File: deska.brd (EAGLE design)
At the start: 100 x 80 mm, 17 parts, among them Q1 BC547, Q2 BC547

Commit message: +
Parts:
- UART: device con-wago-508:W237-132 -> con-wago-508:W237-3E
- moved RELAY 5.08 mm to (5.08, 14.0)
- moved UART 2.54 mm to (5.08, 26.7)
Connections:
- removed net +3V3: BUZZER.2, I2C.2, R1.2, R2.2, R3.2, RELAY.2, TIN.1, TOUT.1, TUT.1, U$1.RAW
- removed net N$8: TIN.2, TOUT.3, TUT.3
- new net +5V: I2C.2, LED.2, R1.2, R2.2, R3.2, RELAY.2, TIN.1, TOUT.1, TUT.1, U$1.RAW
- net GND: now also BUZZER.2, TIN.2, TOUT.3, TUT.3, UART.1; no longer LED.2
- net N$10: now also UART.3; no longer UART.2
- net N$9: now also UART.2; no longer UART.1
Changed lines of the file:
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@@
 <element name="R2" library="rcl" package="0207/7" value="4k7" x="11.43" y="60.96" rot="R90"/>
 <element name="R3" library="rcl" package="0207/7" value="4k7" x="11.43" y="45.72" rot="R90"/>
-<element name="RELAY" library="con-wago-508" package="W237-132" value="" x="5.08" y="19.05" rot="R270">
-<attribute name="OC_NEWARK" value="unknown" x="5.08" y="19.05" size="1.778" layer="27" rot="R270" display="off"/>
-<attribute name="MPN" value="" x="5.08" y="19.05" size="1.778" layer="27" rot="R270" display="off"/>
-<attribute name="MF" value="" x="5.08" y="19.05" size="1.778" layer="27" rot="R270" display="off"/>
-<attribute name="OC_FARNELL" value="unknown" x="5.08" y="19.05" size="1.778" layer="27" rot="R270" display="off"/>
+<element name="RELAY" library="con-wago-508" package="W237-132" value="" x="5.08" y="13.97" rot="R270">
+<attribute name="OC_NEWARK" value="unknown" x="5.08" y="13.97" size="1.778" layer="27" rot="R270" display="off"/>
+<attribute name="MPN" value="" x="5.08" y="13.97" size="1.778" layer="27" rot="R270" display="off"/>
+<attribute name="MF" value="" x="5.08" y="13.97" size="1.778" layer="27" rot="R270" display="off"/>
+<attribute name="OC_FARNELL" value="unknown" x="5.08" y="13.97" size="1.778" layer="27" rot="R270" display="off"/>
 </element>
 <element name="LED" library="con-wago-508" package="W237-132" value="" x="45.72" y="22.86" rot="R270">
@@
 <attribute name="OC_FARNELL" value="unknown" x="5.08" y="41.91" size="1.778" layer="27" rot="R270" display="off"/>
 </element>
-<element name="UART" library="con-wago-508" package="W237-132" value="" x="5.08" y="29.21" rot="R270">
-<attribute name="OC_NEWARK" value="unknown" x="5.08" y="29.21" size="1.778" layer="27" rot="R270" display="off"/>
-<attribute name="MPN" value="" x="5.08" y="29.21" size="1.778" layer="27" rot="R270" display="off"/>
-<attribute name="MF" value="" x="5.08" y="29.21" size="1.778" layer="27" rot="R270" display="off"/>
-<attribute name="OC_FARNELL" value="unknown" x="5.08" y="29.21" size="1.778" layer="27" rot="R270" display="off"/>
-</element>
 <element name="Q1" library="transistor-npn" package="TO92" value="BC547" x="31.75" y="11.43"/>
 <element name="Q2" library="transistor-npn" package="TO92" value="BC547" x="22.86" y="11.43"/>
@@
 <attribute name="OC_FARNELL" value="unknown" x="45.72" y="50.8" size="1.778" layer="27" rot="R90" display="off"/>
 </element>
+<element name="UART" library="con-wago-508" package="W237-3E" value="" x="5.08" y="26.67" rot="R270">
+<attribute name="OC_NEWARK" value="unknown" x="5.08" y="26.67" size="1.778" layer="27" rot="R270" display="off"/>
+<attribute name="MPN" value="" x="5.08" y="26.67" size="1.778" layer="27" rot="R270" display="off"/>
+<attribute name="MF" value="" x="5.08" y="26.67" size="1.778" layer="27" rot="R270" display="off"/>
+<attribute name="OC_FARNELL" value="unknown" x="5.08" y="26.67" size="1.778" layer="27" rot="R270" display="off"/>
+</element>
 </elements>
 <signals>
 <signal name="N$1">
 <contactref element="U$1" pad="D2"/>
+<contactref element="TIN" pad="3"/>
 <contactref element="R1" pad="1"/>
-<contactref element="TIN" pad="3"/>
-<wire x1="11.43" y1="74.93" x2="4.445" y2="67.31" width="0" layer="19" extent="1-1"/>
-<wire x1="19.05" y1="39.37" x2="11.43" y2="74.93" width="0" layer="19" extent="1-1"/>
+<wire x1="4.445" y1="67.31" x2="11.43" y2="74.93" width="0" layer="19" extent="1-1"/>
+<wire x1="19.05" y1="39.37" x2="4.445" y2="67.31" width="0" layer="19" extent="1-1"/>
 </signal>
 <signal name="N$2">
 <contactref element="U$1" pad="D4"/>
+<contactref element="TOUT" pad="2"/>
 <contactref element="R2" pad="1"/>
-<contactref element="TOUT" pad="2"/>
-<wire x1="11.43" y1="57.15" x2="4.445" y2="57.15" width="0" layer="19" extent="1-1"/>
+<wire x1="4.445" y1="57.15" x2="11.43" y2="57.15" width="0" layer="19" extent="1-1"/>
 <wire x1="19.05" y1="34.29" x2="11.43" y2="57.15" width="0" layer="19" extent="1-1"/>
 </signal>
 <signal name="N$3">
 <contactref element="U$1" pad="D5"/>
+<contactref element="TUT" pad="2"/>
 <contactref element="R3" pad="1"/>
-<contactref element="TUT" pad="2"/>
-<wire x1="11.43" y1="41.91" x2="4.445" y2="41.91" width="0" layer="19" extent="1-1"/>
+<wire x1="4.445" y1="41.91" x2="11.43" y2="41.91" width="0" layer="19" extent="1-1"/>
 <wire x1="19.05" y1="31.75" x2="11.43" y2="41.91" width="0" layer="19" extent="1-1"/>
-</signal>
-<signal name="+3V3">
-<contactref element="R3" pad="2"/>
-<contactref element="R2" pad="2"/>
-<contactref element="R1" pad="2"/>
-<contactref element="U$1" pad="RAW"/>
-<contactref element="TIN" pad="1"/>
-<contactref element="TOUT" pad="1"/>
-<contactref element="TUT" pad="1"/>
-<contactref element="RELAY" pad="2"/>
-<contactref element="BUZZER" pad="2"/>
-<contactref element="I2C" pad="2"/>
-<wire x1="45.085" y1="30.48" x2="34.29" y2="49.53" width="0" layer="19" extent="1-1"/>
-<wire x1="11.43" y1="49.53" x2="34.29" y2="49.53" width="0" layer="19" extent="1-1"/>
-<wire x1="4.445" y1="46.99" x2="11.43" y2="49.53" width="0" layer="19" extent="1-1"/>
-<wire x1="4.445" y1="62.23" x2="11.43" y2="49.53" width="0" layer="19" extent="1-1"/>
-<wire x1="11.43" y1="64.77" x2="4.445" y2="62.23" width="0" layer="19" extent="1-1"/>
-<wire x1="11.43" y1="67.31" x2="11.43" y2="64.77" width="0" layer="19" extent="1-1"/>
-<wire x1="4.445" y1="77.47" x2="11.43" y2="67.31" width="0" layer="19" extent="1-1"/>
-<wire x1="4.445" y1="16.51" x2="4.445" y2="46.99" width="0" layer="19" extent="1-1"/>
-<wire x1="46.355" y1="48.26" x2="4.445" y2="16.51" width="0" layer="19" extent="1-1"/>
 </signal>
 <signal name="GND">
 <contactref element="U$1" pad="GND"/>
-<contactref element="LED" pad="2"/>
+<contactref element="UART" pad="1"/>
+<contactref element="BUZZER" pad="2"/>
+<contactref element="I2C" pad="1"/>
 <contactref element="Q2" pad="1"/>
 <contactref element="Q1" pad="1"/>
-<contactref element="I2C" pad="1"/>
-<wire x1="45.085" y1="20.32" x2="34.29" y2="46.99" width="0" layer="19" extent="1-1"/>
-<wire x1="33.02" y1="11.43" x2="45.085" y2="20.32" width="0" layer="19" extent="1-1"/>
+<contactref element="TIN" pad="2"/>
+<contactref element="TOUT" pad="3"/>
+<contactref element="TUT" pad="3"/>
+<wire x1="34.29" y1="46.99" x2="46.355" y2="43.18" width="0" layer="19" extent="1-1"/>
+<wire x1="45.085" y1="30.48" x2="46.355" y2="43.18" width="0" layer="19" extent="1-1"/>
+<wire x1="33.02" y1="11.43" x2="45.085" y2="30.48" width="0" layer="19" extent="1-1"/>
 <wire x1="24.13" y1="11.43" x2="33.02" y2="11.43" width="0" layer="19" extent="1-1"/>
-<wire x1="46.355" y1="43.18" x2="24.13" y2="11.43" width="0" layer="19" extent="1-1"/>
+<wire x1="4.445" y1="31.75" x2="24.13" y2="11.43" width="0" layer="19" extent="1-1"/>
+<wire x1="4.445" y1="36.83" x2="4.445" y2="31.75" width="0" layer="19" extent="1-1"/>
+<wire x1="4.445" y1="52.07" x2="4.445" y2="36.83" width="0" layer="19" extent="1-1"/>
+<wire x1="4.445" y1="72.39" x2="4.445" y2="52.07" width="0" layer="19" extent="1-1"/>
 </signal>
 <signal name="N$5">
@@
 <wire x1="45.085" y1="25.4" x2="26.67" y2="16.51" width="0" layer="19" extent="1-1"/>
 </signal>
-<signal name="N$8">
-<contactref element="TIN" pad="2"/>
-<contactref element="TOUT" pad="3"/>
-<contactref element="TUT" pad="3"/>
-<wire x1="4.445" y1="52.07" x2="4.445" y2="36.83" width="0" layer="19" extent="1-1"/>
-<wire x1="4.445" y1="72.39" x2="4.445" y2="52.07" width="0" layer="19" extent="1-1"/>
-</signal>
 <signal name="N$9">
-<contactref element="UART" pad="1"/>
 <contactref element="U$1" pad="TX0"/>
-<wire x1="19.05" y1="49.53" x2="4.445" y2="31.75" width="0" layer="19" extent="1-1"/>
+<contactref element="UART" pad="2"/>
+<wire x1="4.445" y1="26.67" x2="19.05" y2="49.53" width="0" layer="19" extent="1-1"/>
 </signal>
 <signal name="N$10">
-<contactref element="UART" pad="2"/>
 <contactref element="U$1" pad="RX1"/>
-<wire x1="19.05" y1="46.99" x2="4.445" y2="26.67" width="0" layer="19" extent="1-1"/>
+<contactref element="UART" pad="3"/>
+<wire x1="4.445" y1="21.59" x2="19.05" y2="46.99" width="0" layer="19" extent="1-1"/>
 </signal>
 <signal name="N$12">
@@
 <contactref element="RELAY" pad="1"/>
 <contactref element="Q2" pad="3"/>
-<wire x1="21.59" y1="11.43" x2="4.445" y2="21.59" width="0" layer="19" extent="1-1"/>
+<wire x1="21.59" y1="11.43" x2="4.445" y2="16.51" width="0" layer="19" extent="1-1"/>
 </signal>
 <signal name="N$15">
@@
 <wire x1="30.48" y1="24.13" x2="34.29" y2="29.21" width="0" layer="19" extent="1-1"/>
 </signal>
+<signal name="+5V">
+<contactref element="RELAY" pad="2"/>
+<contactref element="LED" pad="2"/>
+<contactref element="R1" pad="2"/>
+<contactref element="R3" pad="2"/>
+<contactref element="R2" pad="2"/>
+<contactref element="TIN" pad="1"/>
+<contactref element="TUT" pad="1"/>
+<contactref element="TOUT" pad="1"/>
+<contactref element="U$1" pad="RAW"/>
+<contactref element="I2C" pad="2"/>
+<wire x1="34.29" y1="49.53" x2="46.355" y2="48.26" width="0" layer="19" extent="1-1"/>
+<wire x1="11.43" y1="49.53" x2="34.29" y2="49.53" width="0" layer="19" extent="1-1"/>
+<wire x1="4.445" y1="46.99" x2="11.43" y2="49.53" width="0" layer="19" extent="1-1"/>
+<wire x1="4.445" y1="62.23" x2="11.43" y2="49.53" width="0" layer="19" extent="1-1"/>
+<wire x1="11.43" y1="64.77" x2="4.445" y2="62.23" width="0" layer="19" extent="1-1"/>
+<wire x1="11.43" y1="67.31" x2="11.43" y2="64.77" width="0" layer="19" extent="1-1"/>
+<wire x1="4.445" y1="77.47" x2="11.43" y2="67.31" width="0" layer="19" extent="1-1"/>
+<wire x1="45.085" y1="20.32" x2="46.355" y2="48.26" width="0" layer="19" extent="1-1"/>
+<wire x1="4.445" y1="11.43" x2="4.445" y2="46.99" width="0" layer="19" extent="1-1"/>
+</signal>
 </signals>

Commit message: zmeny
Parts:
- removed I2C: (no value), con-wago-508:W237-4P
- added COMMUNIT: (no value), con-wago-508:W237-132
- added I2CDISP, I2CHOUR, I2CKEYB, LEDDISP: (no value), con-wago-508:W237-4P
- moved UART 53.8 mm to (22.9, 77.5), turned to 180 degrees
- moved BUZZER 46.5 mm to (7.62, 6.35)
- moved LED 38.6 mm to (7.62, 16.5)
- moved RELAY 13.0 mm to (7.62, 26.7)
- moved R2 10.5 mm to (14.0, 50.8), turned to 270 degrees
- moved R3 10.5 mm to (14.0, 35.6), turned to 270 degrees
- moved R4 10.2 mm to (16.5, 21.6)
- moved R6 10.2 mm to (40.6, 20.3)
- moved R1 6.84 mm to (14.0, 64.8)
- moved R5 5.12 mm to (25.4, 21.0)
- moved TIN 3.59 mm to (7.62, 69.8)
- moved TOUT 3.59 mm to (7.62, 54.6)
- moved TUT 3.59 mm to (7.62, 39.4)
- moved U$1 2.84 mm to (30.5, 38.1)
- moved Q1 2.84 mm to (34.3, 12.7)
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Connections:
- new net N$17: COMMUNIT.2, U$1.A0
- new net N$8: COMMUNIT.1, U$1.A1
- net +5V: now also I2CDISP.2, I2CHOUR.2, I2CKEYB.2, LEDDISP.2; no longer I2C.2
- net GND: now also I2CDISP.1, I2CHOUR.1, I2CKEYB.1, LEDDISP.1, TIN.3; no longer I2C.1, TIN.2
- net N$1: now also TIN.2; no longer TIN.3
- net N$11: now also I2CDISP.4, I2CHOUR.4, I2CKEYB.4, LEDDISP.4; no longer I2C.4
- net N$12: now also I2CDISP.3, I2CHOUR.3, I2CKEYB.3, LEDDISP.3; no longer I2C.3
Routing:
- net GND: track 0.00 -> 268.1 mm
- net +5V: track 0.00 -> 240.2 mm
- net N$12: track 0.00 -> 98.0 mm
- net N$11: track 0.00 -> 87.7 mm
- net N$8: track 0.00 -> 45.6 mm
- net N$1: track 0.00 -> 43.8 mm
- net N$17: track 0.00 -> 42.6 mm
- net N$2: track 0.00 -> 33.7 mm
- net N$14: track 0.00 -> 32.2 mm
- net N$10: track 0.00 -> 32.0 mm
- net N$15: track 0.00 -> 29.8 mm
- net N$9: track 0.00 -> 28.9 mm
- net N$3: track 0.00 -> 19.2 mm
- net N$16: track 0.00 -> 10.2 mm
- net N$6: track 0.00 -> 10.1 mm
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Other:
- board size 100 x 80 mm -> 55.5 x 83.8 mm

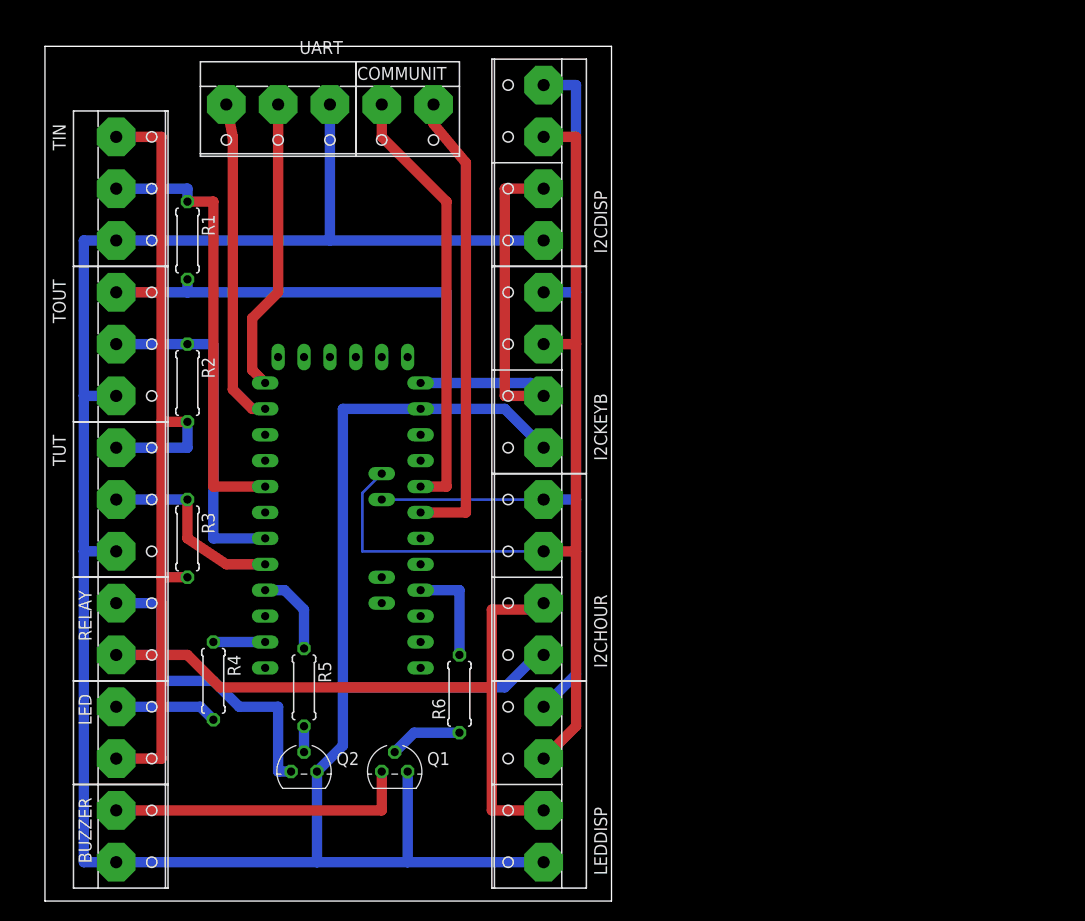
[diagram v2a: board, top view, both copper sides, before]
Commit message: uprava desky, prida konektor pro napajeni
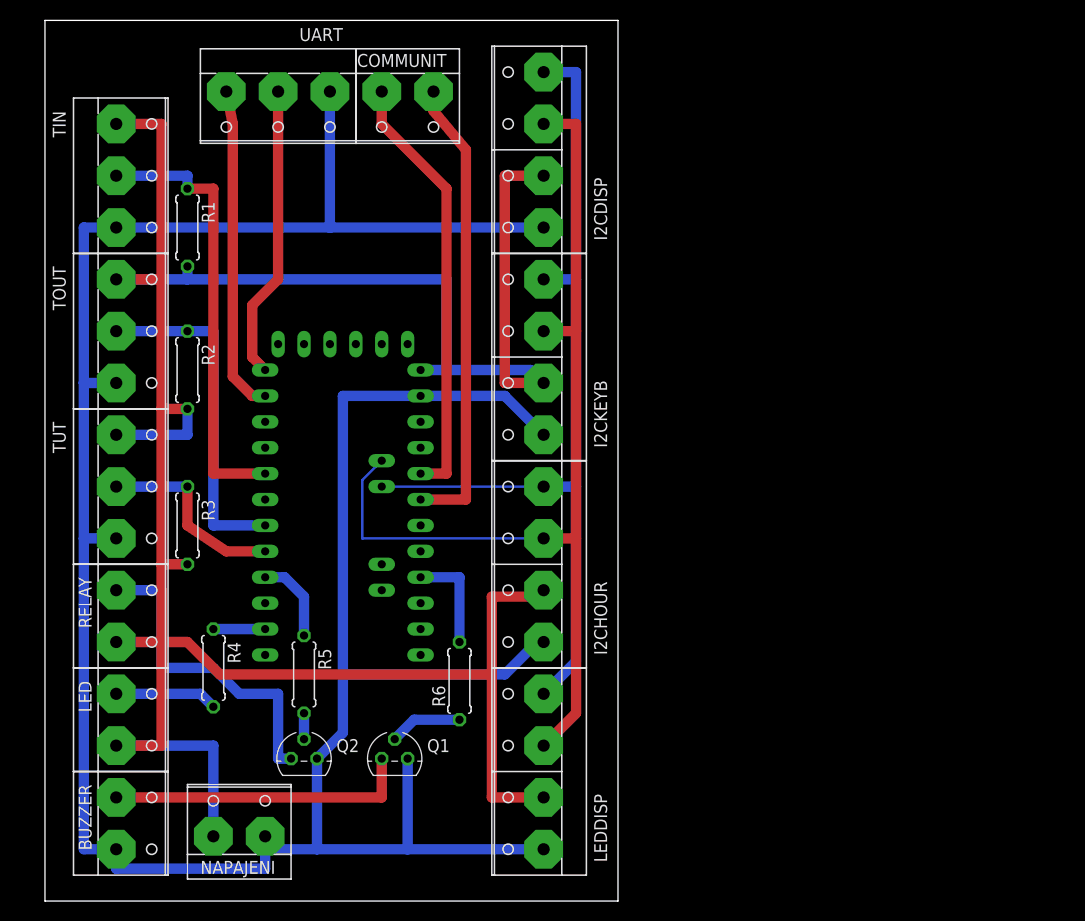
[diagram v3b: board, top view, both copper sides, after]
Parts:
- added NAPAJENI: (no value), con-wago-508:W237-132
- moved R1 1.27 mm to (14.0, 66.0)
- moved TIN 1.27 mm to (7.62, 71.1)
- moved I2CHOUR 1.27 mm to (48.3, 33.0)
- moved I2CKEYB 1.27 mm to (48.3, 53.3)
- moved R2 1.27 mm to (14.0, 52.1)
- moved R5 1.27 mm to (25.4, 22.2)
- moved TOUT 1.27 mm to (7.62, 55.9)
- moved TUT 1.27 mm to (7.62, 40.6)
- moved Q1 1.27 mm to (34.3, 14.0)
- moved Q2 1.27 mm to (25.4, 14.0)
- moved BUZZER 1.27 mm to (7.62, 7.62)
- moved LED 1.27 mm to (7.62, 17.8)
- moved LEDDISP 1.27 mm to (48.3, 12.7)
- moved R4 1.27 mm to (16.5, 22.9)
- moved R6 1.27 mm to (40.6, 21.6)
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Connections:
- net +5V: now also NAPAJENI.1
- net GND: now also NAPAJENI.2
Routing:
- net +5V: track 240.2 -> 258.6 mm
- net GND: track 268.1 -> 274.5 mm
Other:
- board size 55.5 x 83.8 mm -> 56.2 x 86.3 mm

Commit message: +upraveny DPS DPS objednany 27.4.2016
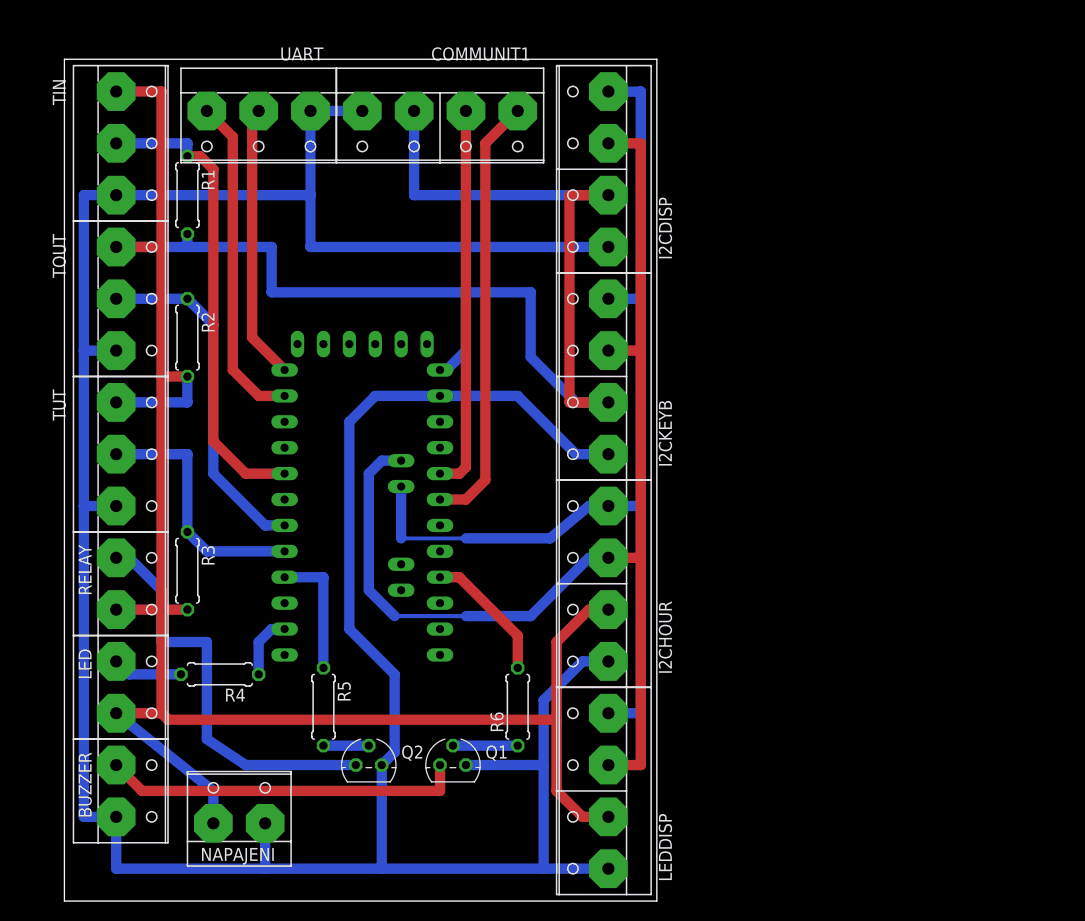
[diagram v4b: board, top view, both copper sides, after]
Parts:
- removed COMMUNIT: (no value), con-wago-508:W237-132
- added COMMUNIT1: (no value), con-wago-508:W237-4P
- moved I2CDISP 6.63 mm to (54.6, 71.8)
- moved I2CHOUR 6.63 mm to (54.6, 31.1)
- moved I2CKEYB 6.63 mm to (54.6, 51.4)
- moved LEDDISP 6.63 mm to (54.6, 10.8)
- moved Q2 6.38 mm to (31.8, 13.3)
- moved R6 6.25 mm to (46.4, 19.1)
- moved Q1 5.75 mm to (40.0, 13.3)
- moved R3 4.45 mm to (14.0, 32.4)
- moved R5 3.70 mm to (27.3, 19.1)
- moved BUZZER 3.17 mm to (7.62, 10.8)
- moved LED 3.17 mm to (7.62, 21.0)
- moved R1 3.17 mm to (14.0, 69.2)
- moved R2 3.17 mm to (14.0, 55.2)
- moved RELAY 3.17 mm to (7.62, 31.1)
- moved TIN 3.17 mm to (7.62, 74.3)
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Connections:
- net +5V: now also COMMUNIT1.3
- net GND: now also COMMUNIT1.4
- net N$17: now also COMMUNIT1.2; no longer COMMUNIT.2
- net N$8: now also COMMUNIT1.1; no longer COMMUNIT.1
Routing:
- net +5V: track 258.6 -> 301.3 mm
- net GND: track 274.5 -> 305.2 mm
- net N$12: track 98.0 -> 115.7 mm
- net N$11: track 87.7 -> 100.2 mm
- net N$14: track 32.2 -> 40.2 mm
- net N$3: track 19.2 -> 24.9 mm
- net N$15: track 29.8 -> 35.3 mm
- net N$17: track 42.6 -> 37.7 mm
- net N$4: track 8.41 -> 12.7 mm
- net N$6: track 10.1 -> 6.88 mm
- net N$16: track 10.2 -> 13.2 mm
- net N$1: track 43.8 -> 46.3 mm
- net N$8: track 45.6 -> 43.4 mm
- net N$9: track 28.9 -> 26.9 mm
- net N$13: track 2.54 -> 4.45 mm
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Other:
- board size 56.2 x 86.3 mm -> 58.1 x 82.5 mm
